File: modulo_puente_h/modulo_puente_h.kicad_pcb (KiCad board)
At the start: 2 copper layers, 63 x 50 mm, 16 parts, among them J1 Conn_01x07_Pin, M1 Motor_IZQ, M2 Motor_DER, U1 L298N

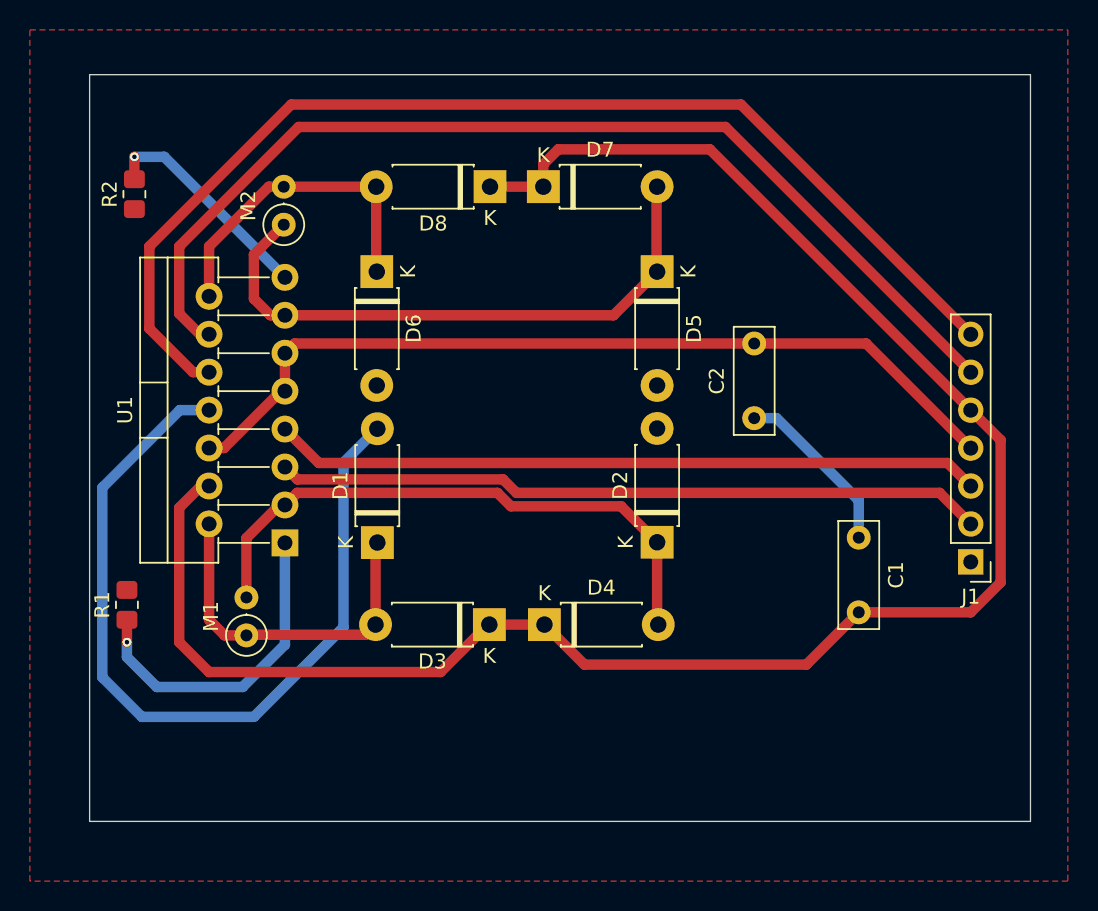
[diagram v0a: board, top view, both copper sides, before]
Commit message: refactor(puente-h): Achico la placa
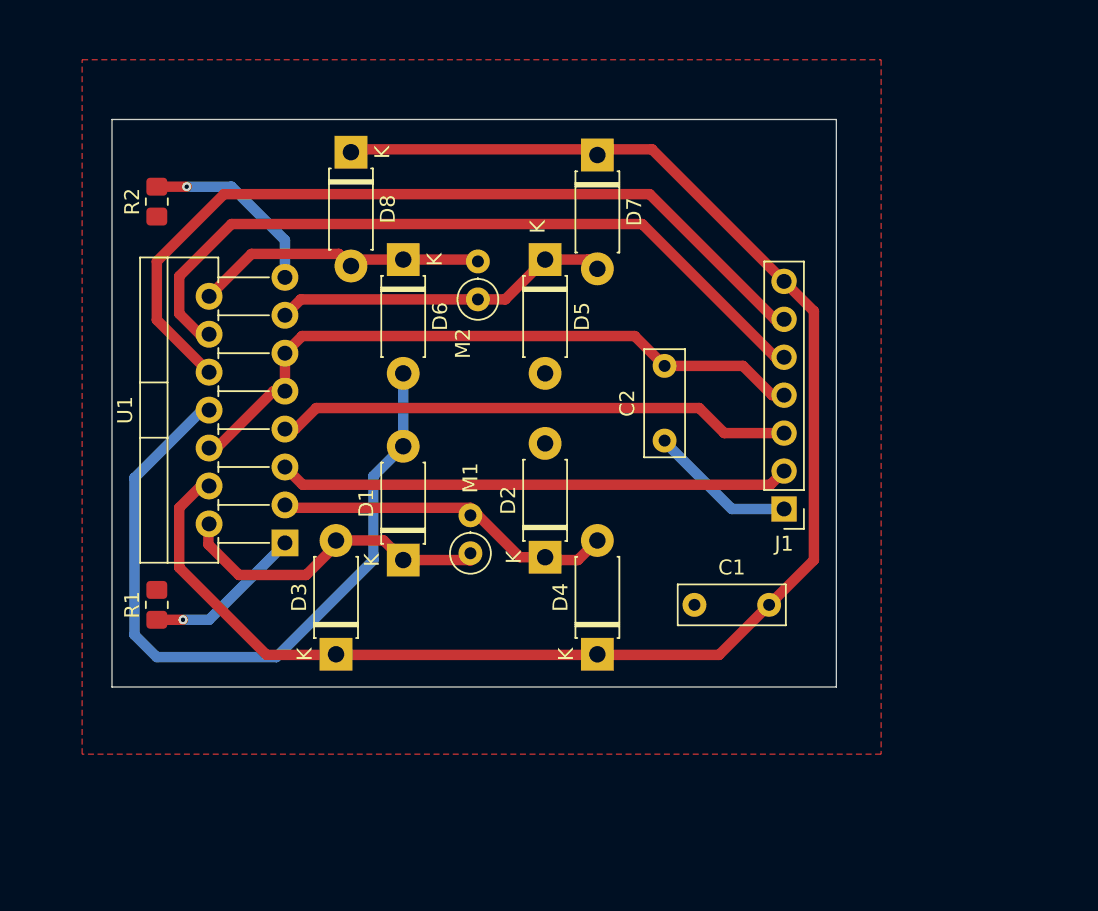
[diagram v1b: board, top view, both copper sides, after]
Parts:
- moved M1 16.0 mm to (75.5, 76.0)
- moved M2 13.9 mm to (76.0, 59.0)
- moved J1 13.0 mm to (96.5, 73.1)
- moved C1 11.9 mm to (90.5, 79.5), turned to 0 degrees
- moved D3 10.5 mm to (66.5, 82.8), turned to 90 degrees
- moved D8 9.59 mm to (67.5, 49.2), turned to -90 degrees
- moved D2 7.57 mm to (80.5, 76.3)
- moved D5 7.54 mm to (80.5, 56.4)
- moved C2 6.18 mm to (88.5, 68.5)
- moved D7 4.20 mm to (84.0, 49.4), turned to -90 degrees
- moved D4 4.06 mm to (84.0, 82.8), turned to 90 degrees
- moved D1 2.09 mm to (71.0, 76.5)
- moved R1 2.00 mm to (54.5, 79.5)
- moved D6 1.95 mm to (71.0, 56.4)
- moved R2 1.58 mm to (54.5, 52.5)
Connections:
- J1 pad 5: /Salida Regulador -> /Entrada 2 Motor B
- J1 pad 6: /Entrada 2 Motor B -> /Entrada 1 Motor B
- J1 pad 7: /Entrada 1 Motor B -> /Salida Regulador
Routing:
- net /Entrada 1 Motor B: track 76.2 -> 56.2 mm
- net /Entrada 2 Motor B: track 70.2 -> 50.7 mm
- net /Salida Regulador: track 125.8 -> 106.5 mm
- net Net-(D5-K): track 40.1 -> 22.7 mm
- net Net-(D2-K): track 39.6 -> 24.0 mm
- net +5V: track 58.3 -> 44.7 mm
- net /Entrada 1 Motor A: track 47.6 -> 34.3 mm
- net /Entrada 2 Motor A: track 47.5 -> 34.7 mm
- net Net-(U1-SENSE_A): track 21.9 -> 10.5 mm
- net GND: track 67.9 -> 60.0 mm
- net Net-(D6-K): track 21.9 -> 19.4 mm
- net Net-(U1-SENSE_B): track 14.9 -> 12.6 mm
- net Net-(D1-K): track 23.8 -> 21.5 mm
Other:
- board size 63 x 50 mm -> 48.5 x 38 mm
